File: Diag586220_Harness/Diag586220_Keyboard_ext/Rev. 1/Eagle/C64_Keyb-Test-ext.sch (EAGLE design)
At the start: 13 parts, among them IC1 4066N, IC2 4066N, J1 BL1-85AXX-20U, Q1 BC547B

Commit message: Silk Screen Update
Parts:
- added U$19: OPEN_SOURCE_HW, Logo:OPEN_SOURCE_HW
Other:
- note added: "http://github.com/svenpetersen1965"
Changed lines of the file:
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@@
 <layer number="250" name="Descript" color="7" fill="1" visible="no" active="no"/>
 <layer number="251" name="SMDround" color="7" fill="1" visible="no" active="no"/>
+<layer number="252" name="BR-BS" color="7" fill="1" visible="no" active="yes"/>
+<layer number="253" name="BR-LS" color="7" fill="1" visible="no" active="yes"/>
 <layer number="254" name="OrgLBR" color="7" fill="1" visible="no" active="no"/>
 <layer number="255" name="Accent" color="7" fill="1" visible="yes" active="yes"/>
@@
 <part name="R5" library="DISCRETE" deviceset="RES04" device="" value="10k"/>
 <part name="U$18" library="!pownet" deviceset="+5V" device=""/>
+<part name="U$19" library="Logo" deviceset="OPEN_SOURCE_HW" device=""/>
 </parts>
 <sheets>
@@
 feedbacks switched
 on when J2 open</text>
+<text x="170.18" y="6.35" size="2.54" layer="95">http://github.com/svenpetersen1965</text>
 </plain>
 <instances>
@@
 <attribute name="VALUE" x="120.015" y="69.215" size="1.524" layer="96"/>
 </instance>
+<instance part="U$19" gate="G$1" x="128.27" y="6.35" smashed="yes"/>
 </instances>
 <busses>

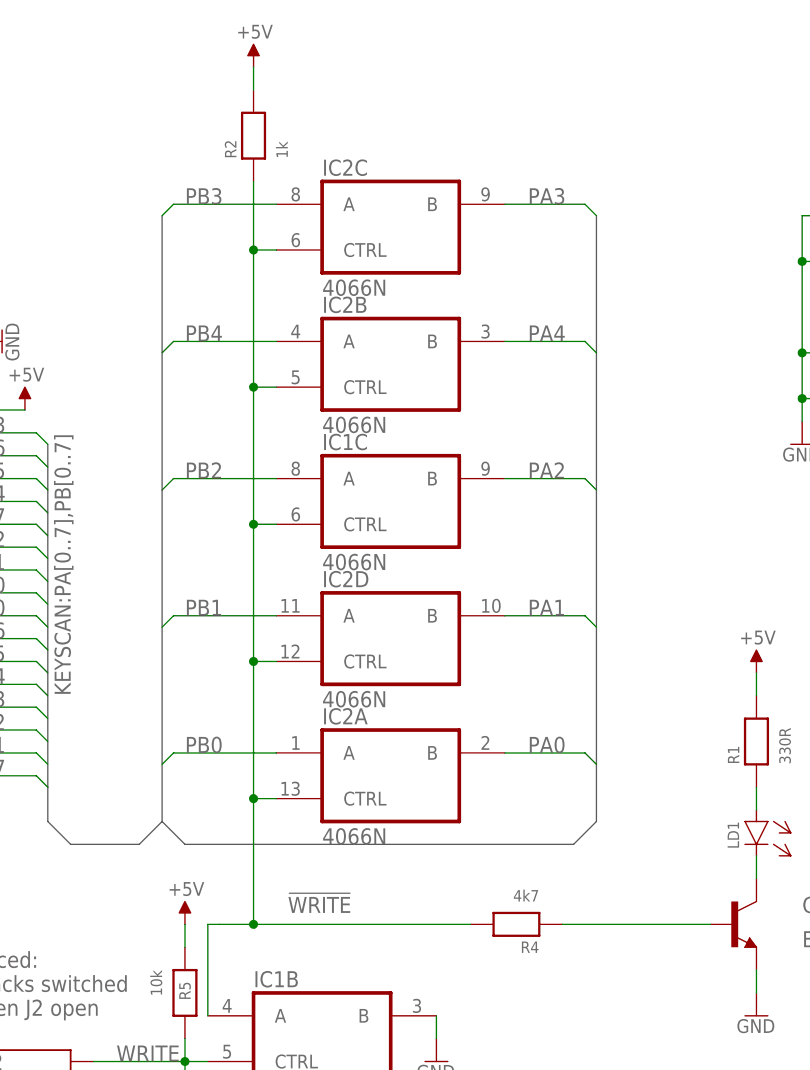
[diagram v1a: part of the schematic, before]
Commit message: BOM v1.1
R2 and R4 values are changed
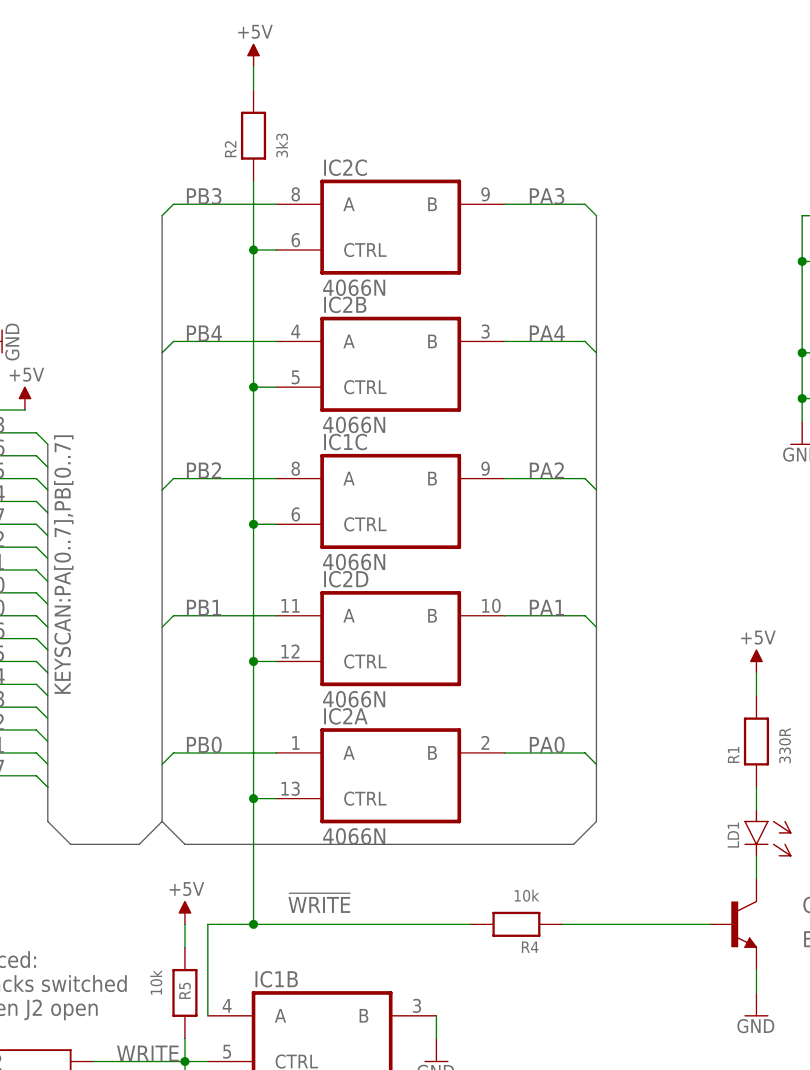
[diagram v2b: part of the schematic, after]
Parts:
- R2: value 1k -> 3k3
- R4: value 4k7 -> 10k
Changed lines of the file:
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@@
 <?xml version="1.0" encoding="utf-8"?>
 <!DOCTYPE eagle SYSTEM "eagle.dtd">
-<eagle version="9.5.2">
+<eagle version="9.6.2">
 <drawing>
 <settings>
@@
 <part name="R1" library="DISCRETE" deviceset="RES04" device="" value="330R"/>
 <part name="R3" library="DISCRETE" deviceset="RES04" device="" value="n/a"/>
-<part name="R2" library="DISCRETE" deviceset="RES04" device="" value="1k"/>
+<part name="R2" library="DISCRETE" deviceset="RES04" device="" value="3k3"/>
 <part name="U$10" library="!pownet" deviceset="GND" device=""/>
 <part name="U$11" library="!pownet" deviceset="GND" device=""/>
@@
 <part name="U$16" library="!pownet" deviceset="GND" device=""/>
 <part name="Q1" library="Transistoren" deviceset="BC547*" device="" technology="B"/>
-<part name="R4" library="DISCRETE" deviceset="RES04" device="" value="4k7"/>
+<part name="R4" library="DISCRETE" deviceset="RES04" device="" value="10k"/>
 <part name="C1" library="DISCRETE" deviceset="CAP01" device="" value="100n"/>
 <part name="C2" library="DISCRETE" deviceset="CAP01" device="" value="100n"/>
